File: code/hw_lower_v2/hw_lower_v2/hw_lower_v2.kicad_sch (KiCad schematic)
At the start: 6 parts

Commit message: further lower board sch work
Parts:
- added J1: Conn_01x20_Pin, symbol Connector:Conn_01x20_Pin
- added J2: Conn_01x04_Pin, symbol Connector:Conn_01x04_Pin
- R25, R26, R27, R28, R29, R30: footprint (none) -> Resistor_SMD:R_0603_1608Metric
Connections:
- net +3.3V: now also J1.4 (Pin_4)
- net AC/AC_RELAY_PWM: now also J1.14 (Pin_14)
- net AC/AC_RELAY_SENSE: now also J1.13 (Pin_13)
- net AC/GFCI_CALIBRATE: now also J1.11 (Pin_11)
- net AC/GFCI_FAULT: now also J1.10 (Pin_10)
- net AC/GFCI_TEST: now also J1.12 (Pin_12)
- net AC/POWER_MEASUREMENT_CLK: now also J1.9 (Pin_9)
- net AC/POWER_MEASUREMENT_INFO: now also J1.6 (Pin_6)
- net AC/POWER_MEASUREMENT_RX: now also J1.8 (Pin_8)
- net AC/POWER_MEASUREMENT_TX: now also J1.7 (Pin_7)
- net BV0: now also J1.1 (Pin_1)
- net BV1: now also J1.2 (Pin_2)
- net BV2: now also J1.3 (Pin_3)
- net EVSE control and status/CONTROL_PILOT_OUT: now also J2.1 (Pin_1)
- net EVSE control and status/CONTROL_PILOT_PWM: now also J1.15 (Pin_15)
- net EVSE control and status/CONTROL_PILOT_SENSE: now also J1.16 (Pin_16)
- net EVSE control and status/LOCK_A: now also J1.19 (Pin_19)
- net EVSE control and status/LOCK_A_OUT: now also J2.3 (Pin_3)
- net EVSE control and status/LOCK_B: now also J1.18 (Pin_18)
- net EVSE control and status/LOCK_B_OUT: now also J2.4 (Pin_4)
- net EVSE control and status/PROXIMITY_PILOT: now also J2.2 (Pin_2)
- net EVSE control and status/PROXIMITY_PILOT_SENSE: now also J1.17 (Pin_17)
- net GND: now also J1.20 (Pin_20)
- new net +12V: J1.5 (Pin_5)
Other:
- note added: "Add test points ? Find voltage transformer calculate measurement components create relay footprint create RCD footprint create -12V circuit Add flash for lower board calibration and testing AC input protection Proximity pilot pullup value calculation Proximity pilot input protection Motor output voltage protection ? Select AC connections Select nonpolarised capacitors Select interboard connectors"
- note added: "BOARD VERSION: V0"
- note added: "Pinout depends on the connector"
- note removed: "BOARD VERSION"
- moved on the sheet: R25, R26, R27, R28, R29, R30

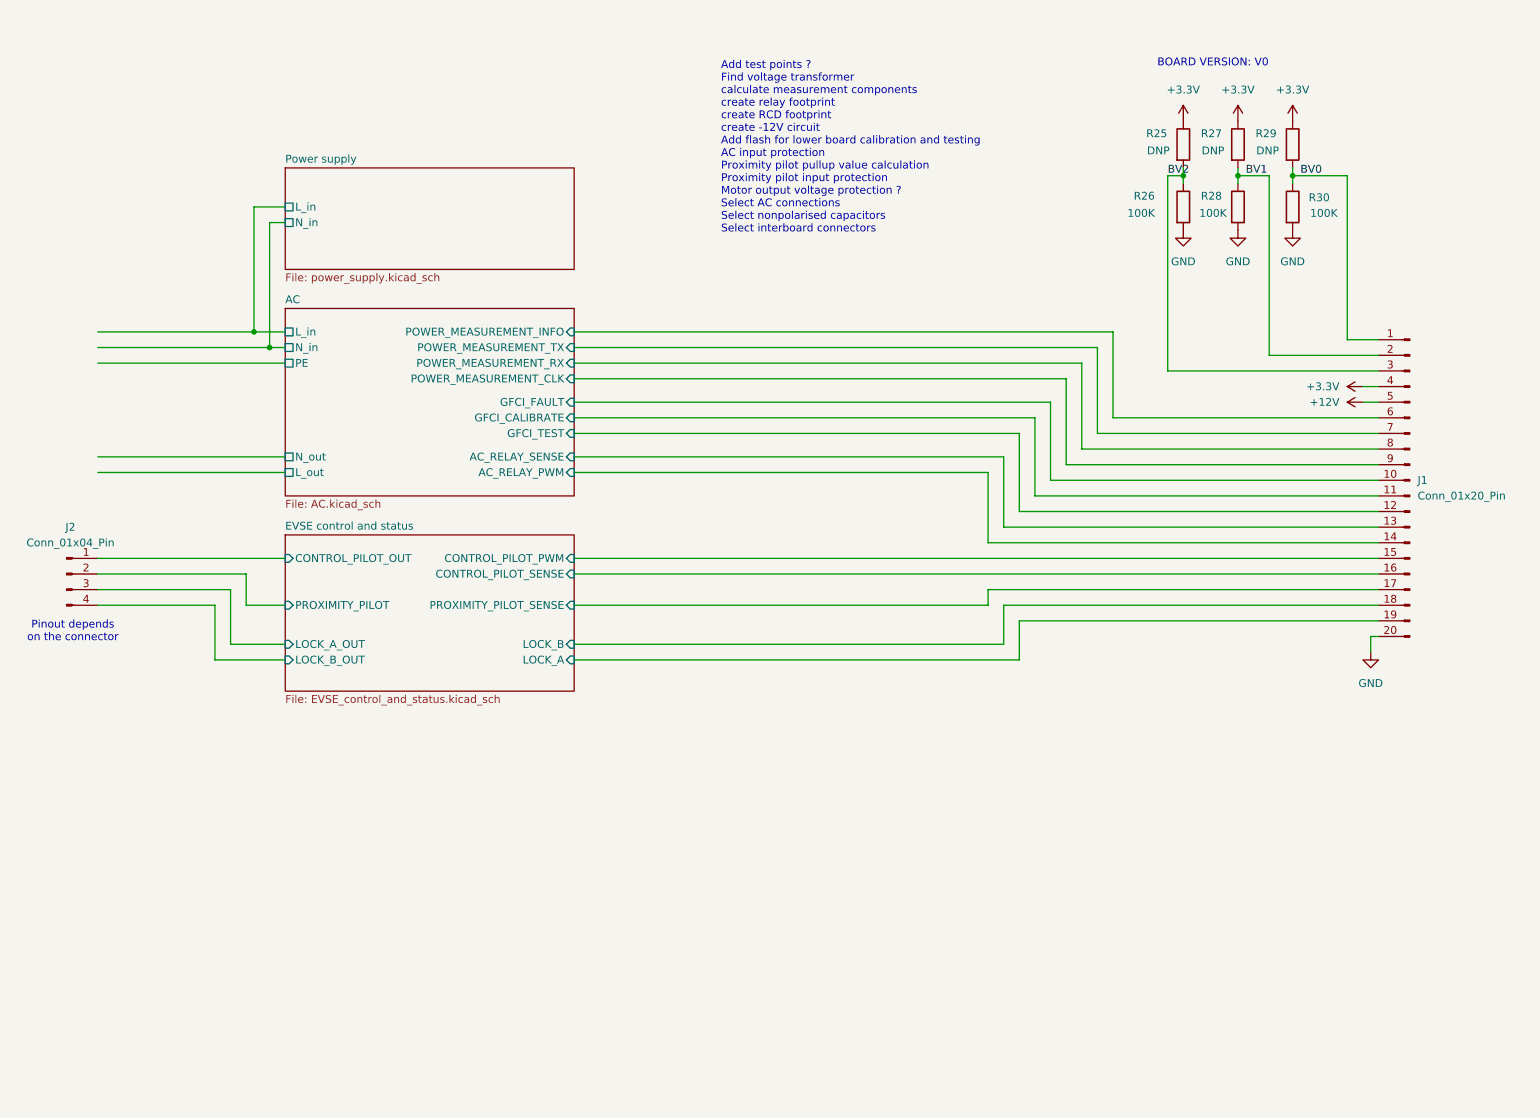
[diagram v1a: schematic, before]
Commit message: add 12V voltage inverter and polish
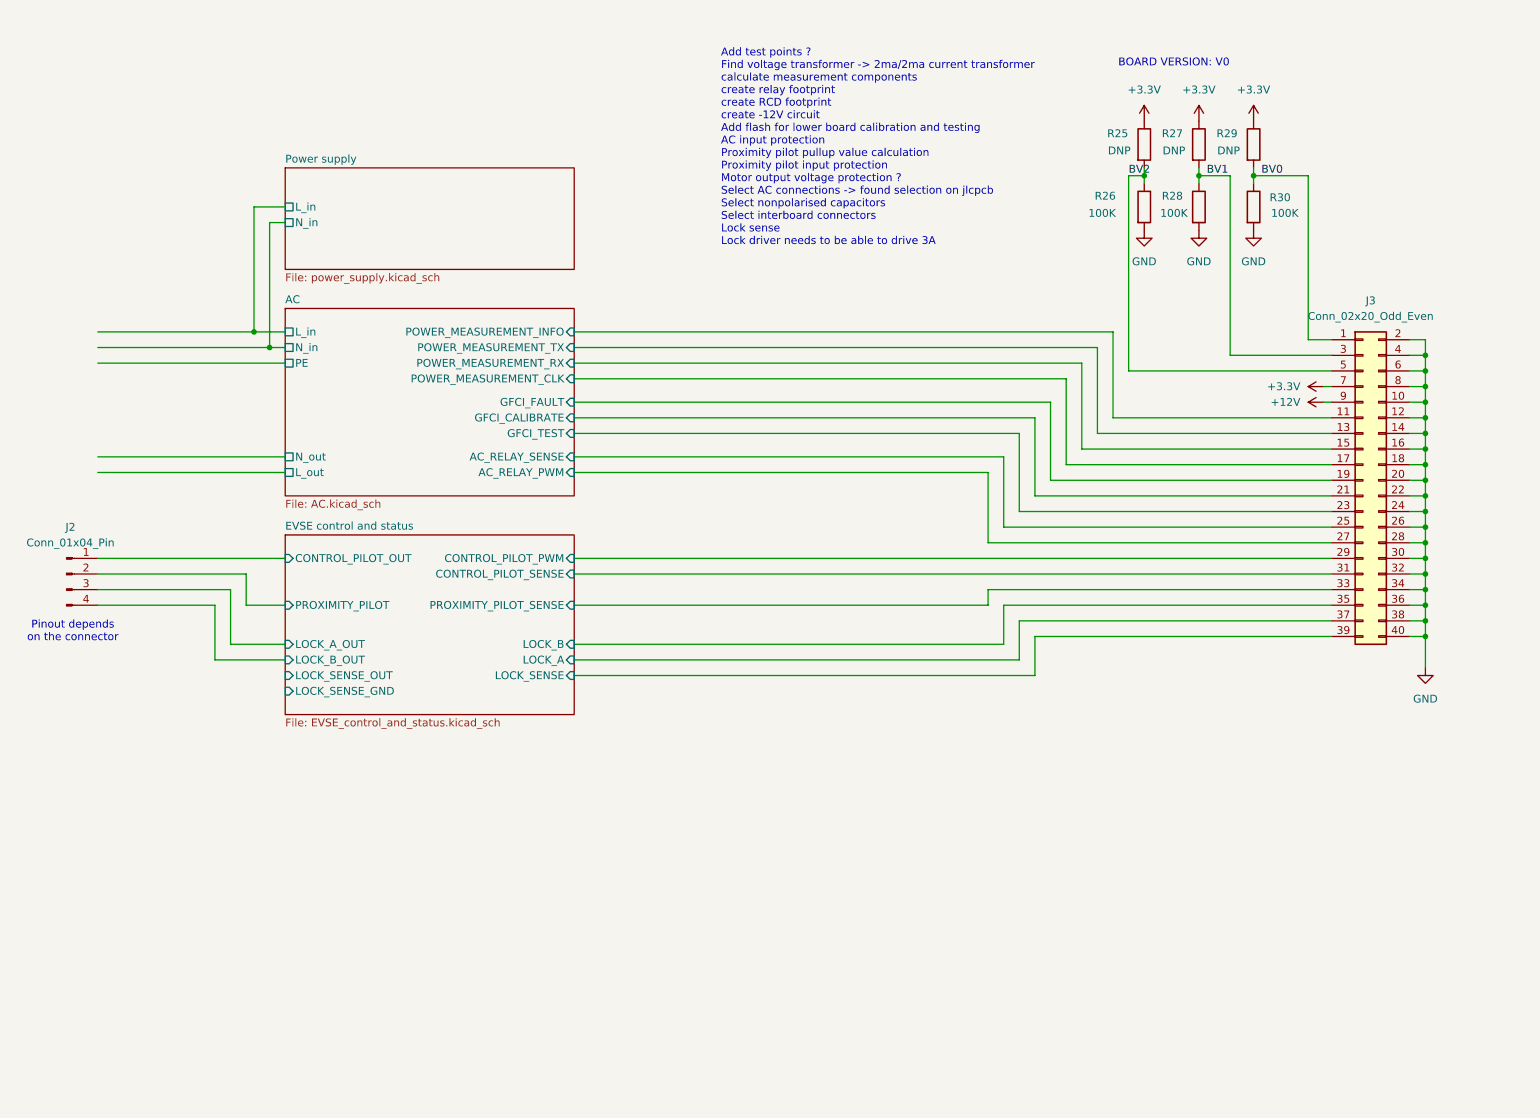
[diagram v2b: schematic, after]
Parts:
- removed J1: Conn_01x20_Pin, symbol Connector:Conn_01x20_Pin
- added J3: Conn_02x20_Odd_Even, symbol Connector_Generic:Conn_02x20_Odd_Even
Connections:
- net +12V: now also J3.9 (Pin_9)
- net +3.3V: now also J3.7 (Pin_7)
- net AC/AC_RELAY_PWM: now also J3.27 (Pin_27)
- net AC/AC_RELAY_SENSE: now also J3.25 (Pin_25)
- net AC/GFCI_CALIBRATE: now also J3.21 (Pin_21)
- net AC/GFCI_FAULT: now also J3.19 (Pin_19)
- net AC/GFCI_TEST: now also J3.23 (Pin_23)
- net AC/POWER_MEASUREMENT_CLK: now also J3.17 (Pin_17)
- net AC/POWER_MEASUREMENT_INFO: now also J3.11 (Pin_11)
- net AC/POWER_MEASUREMENT_RX: now also J3.15 (Pin_15)
- net AC/POWER_MEASUREMENT_TX: now also J3.13 (Pin_13)
- net BV0: now also J3.1 (Pin_1)
- net BV1: now also J3.3 (Pin_3)
- net BV2: now also J3.5 (Pin_5)
- net EVSE control and status/CONTROL_PILOT_PWM: now also J3.29 (Pin_29)
- net EVSE control and status/CONTROL_PILOT_SENSE: now also J3.31 (Pin_31)
- net EVSE control and status/LOCK_A: now also J3.37 (Pin_37)
- net EVSE control and status/LOCK_B: now also J3.35 (Pin_35)
- net EVSE control and status/PROXIMITY_PILOT_SENSE: now also J3.33 (Pin_33)
- net GND: now also J3.10 (Pin_10), J3.12 (Pin_12), J3.14 (Pin_14), J3.16 (Pin_16), J3.18 (Pin_18), J3.2 (Pin_2), J3.20 (Pin_20), J3.22 (Pin_22), J3.24 (Pin_24), J3.26 (Pin_26), J3.28 (Pin_28), J3.30 (Pin_30), J3.32 (Pin_32), J3.34 (Pin_34), J3.36 (Pin_36), J3.38 (Pin_38), J3.4 (Pin_4), J3.40 (Pin_40), J3.6 (Pin_6), J3.8 (Pin_8)
- new net EVSE control and status/LOCK_SENSE: J3.39 (Pin_39)
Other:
- sheet EVSE control and status ports: added LOCK_SENSE, LOCK_SENSE_GND, LOCK_SENSE_OUT; removed none
- note added: "Add test points ? Find voltage transformer -> 2ma/2ma current transformer calculate measurement components create relay footprint create RCD footprint create -12V circuit Add flash for lower board calibration and testing AC input protection Proximity pilot pullup value calculation Proximity pilot input protection Motor output voltage protection ? Select AC connections -> found selection on jlcpcb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"
- note removed: "Add test points ? Find voltage transformer calculate measurement components create relay footprint create RCD footprint create -12V circuit Add flash for lower board calibration and testing AC input protection Proximity pilot pullup value calculation Proximity pilot input protection Motor output voltage protection ? Select AC connections Select nonpolarised capacitors Select interboard connectors"
- moved on the sheet: R25, R26, R27, R28, R29, R30

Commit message: schematic is done
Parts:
- removed J2: Conn_01x04_Pin, symbol Connector:Conn_01x04_Pin
- added J10, J11, J12, J13, J14, J9: Screw_Terminal_01x01, symbol Connector:Screw_Terminal_01x01
- added J2: Conn_01x06_Pin, symbol Connector:Conn_01x06_Pin
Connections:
- net +12V: now also J3.1 (Pin_1); no longer J3.9 (Pin_9)
- net +3.3V: now also J3.5 (Pin_5); no longer J3.7 (Pin_7)
- net AC/L_in: now also J9.1 (Pin_1)
- net AC/L_out: now also J14.1 (Pin_1)
- net AC/N_in: now also J10.1 (Pin_1)
- net AC/N_out: now also J13.1 (Pin_1)
- net AC/PE: now also J11.1 (Pin_1), J12.1 (Pin_1)
- net BV0: now also J3.36 (Pin_36); no longer J3.1 (Pin_1)
- net BV1: now also J3.38 (Pin_38); no longer J3.3 (Pin_3)
- net BV2: now also J3.40 (Pin_40); no longer J3.5 (Pin_5)
- net EVSE control and status/CONTROL_PILOT_OUT: now also J2.1 (Pin_1)
- net EVSE control and status/LOCK_A_OUT: now also J2.3 (Pin_3)
- net EVSE control and status/LOCK_B_OUT: now also J2.4 (Pin_4)
- net EVSE control and status/LOCK_SENSE_GND: now also J2.6 (Pin_6)
- net EVSE control and status/LOCK_SENSE_OUT: now also J2.5 (Pin_5)
- net EVSE control and status/PROXIMITY_PILOT: now also J2.2 (Pin_2)
- net GND: no longer J3.36 (Pin_36), J3.38 (Pin_38), J3.40 (Pin_40)
- new net +5V: J3.3 (Pin_3)
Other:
- note added: "SCH: - Add test points ? X Find voltage transformer -> 2ma/2ma current transformer X calculate measurement components X create -12V circuit - Add flash for lower board calibration and testing X AC input protection X Proximity pilot pullup value calculation X Proximity pilot input protection - Motor output voltage protection ? X Select interboard connectors X Lock sense - Lock driver needs to be a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"
- note removed: "Add test points ? Find voltage transformer -> 2ma/2ma current transformer calculate measurement components create relay footprint create RCD footprint create -12V circuit Add flash for lower board calibration and testing AC input protection Proximity pilot pullup value calculation Proximity pilot input protection Motor output voltage protection ? Select AC connections -> found selection on jlcpcb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"
- moved on the sheet: R25, R26, R27, R28, R29, R30

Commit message: finishing up sch and creating footprints
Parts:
- added FID1, FID2: Fiducial, symbol Mechanical:Fiducial
- added H1, H2, H3, H4, H5, H6: MountingHole_Pad, symbol Mechanical:MountingHole_Pad
- J1: renamed from J9; JLCPCB Part # (none) -> C481447
- J2: renamed from J10; JLCPCB Part # (none) -> C481447
- J3: renamed from J11; JLCPCB Part # (none) -> C481447
- J4: renamed from J12; JLCPCB Part # (none) -> C481447
- J5: renamed from J13; JLCPCB Part # (none) -> C481447
- J6: renamed from J14; JLCPCB Part # (none) -> C481447
- renumbered J2 to J7, J3 to J8, R25 to R1, R26 to R2, R27 to R3, R28 to R4, R29 to R5, R30 to R6

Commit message: wip
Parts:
- J1, J2, J3, J4, J5, J6: JLCPCB Part # C481447 -> (none); LCSC (none) -> C481447
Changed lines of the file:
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@@
 			)
 		)
-		(property "JLCPCB Part #" "C481447"
+		(property "LCSC" "C481447"
 			(at 36.83 90.17 0)
 			(effects
@@
 			)
 		)
-		(property "JLCPCB Part #" "C481447"
+		(property "LCSC" "C481447"
 			(at 36.83 72.39 0)
 			(effects
@@
 			)
 		)
-		(property "JLCPCB Part #" "C481447"
+		(property "LCSC" "C481447"
 			(at 36.83 87.63 0)
 			(effects
@@
 			)
 		)
-		(property "JLCPCB Part #" ""
-			(at 237.49 137.16 0)
-			(effects
-				(font
-					(size 1.27 1.27)
-				)
-				(hide yes)
-			)
-		)
 		(pin "1"
 		)
@@
 			)
 		)
-		(property "JLCPCB Part #" ""
-			(at 237.49 147.32 0)
-			(effects
-				(font
-					(size 1.27 1.27)
-				)
-				(hide yes)
-			)
-		)
 		(pin "1"
 		)
@@
 			)
 		)
-		(property "JLCPCB Part #" "C481447"
+		(property "LCSC" "C481447"
 			(at 36.83 67.31 0)
 			(effects
@@
 			)
 		)
-		(property "JLCPCB Part #" ""
-			(at 36.83 109.22 0)
-			(effects
-				(font
-					(size 1.27 1.27)
-				)
-				(hide yes)
-			)
-		)
 		(pin "2"
 		)
@@
 			)
 		)
-		(property "JLCPCB Part #" ""
-			(at 255.27 147.32 0)
-			(effects
-				(font
-					(size 1.27 1.27)
-				)
-				(hide yes)
-			)
-		)
 		(pin "1"
 		)
@@
 			)
 		)
-		(property "JLCPCB Part #" ""
-			(at 247.65 91.44 0)
-			(effects
-				(font
-					(size 1.27 1.27)
-				)
-				(hide yes)
-			)
-		)
 		(pin "37"
 		)
@@
 			)
 		)
-		(property "JLCPCB Part #" ""
-			(at 246.38 137.16 0)
-			(effects
-				(font
-					(size 1.27 1.27)
-				)
-				(hide yes)
-			)
-		)
 		(pin "1"
 		)
@@
 			)
 		)
-		(property "JLCPCB Part #" "C481447"
+		(property "LCSC" "C481447"
 			(at 36.83 85.09 0)
 			(effects
@@
 			)
 		)
-		(property "JLCPCB Part #" "C481447"
+		(property "LCSC" "C481447"
 			(at 36.83 69.85 0)
 			(effects
@@
 			)
 		)
-		(property "JLCPCB Part #" ""
-			(at 246.38 147.32 0)
-			(effects
-				(font
-					(size 1.27 1.27)
-				)
-				(hide yes)
-			)
-		)
 		(pin "1"
 		)
@@
 			(at 255.27 137.16 0)
 			(effects
-				(font
-					(size 1.27 1.27)
-				)
-				(hide yes)
-			)
-		)
-		(property "JLCPCB Part #" ""
-			(at 255.27 137.16 0)
-			(effects
